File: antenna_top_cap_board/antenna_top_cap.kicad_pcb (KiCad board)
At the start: 4 copper layers, 100 x 100 mm, 61 parts, among them IC1 PCT2075DP,118, J1 Battery Charge Bypass, J10 USB_B_Micro, J11 USB_B_Micro, J13 USB_B_Micro, J14 BM04B-SRSS-TB(LF)(SN), J15 USB_B_Micro, J16 BM04B-SRSS-TB(LF)(SN), J17 BM04B-SRSS-TB(LF)(SN), J18 BM04B-SRSS-TB(LF)(SN)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

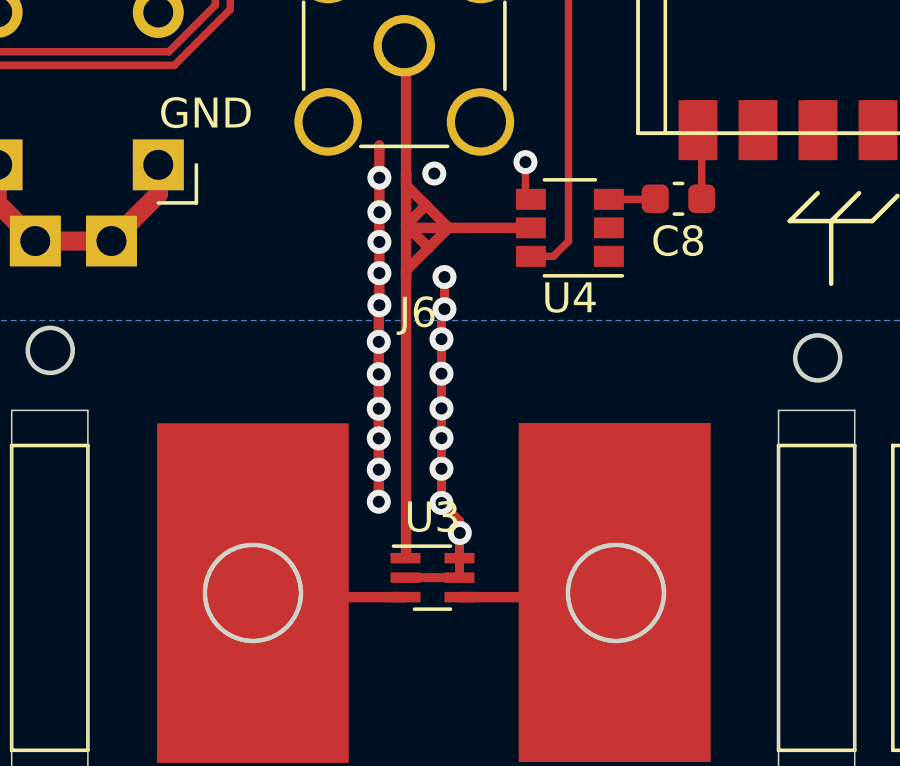
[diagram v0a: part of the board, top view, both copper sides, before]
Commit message: Added Jumper to Aux RF Line
Added an 0603 Jumper to break the Aux RF connection when not in use
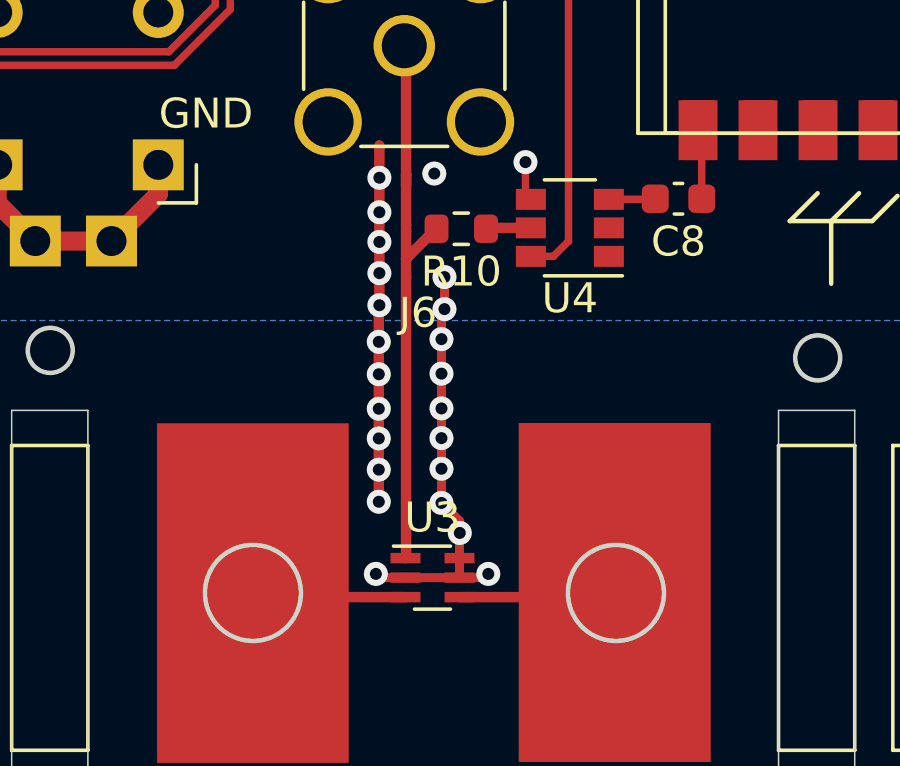
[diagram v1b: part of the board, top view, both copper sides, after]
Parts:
- added R10: DNI, Resistor_SMD:R_0603_1608Metric, F.Cu at (166.4, 123.8)
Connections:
- J5 pad 1: Balun -> Net-(J5-In)
- U3 pad 1: Balun -> Net-(J5-In)
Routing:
- net Balun: track 27.0 -> 1.51 mm
- net Net-(J5-In): track 0.00 -> 18.1 mm
- net GND: track 208.4 -> 210.5 mm, vias 38 -> 40

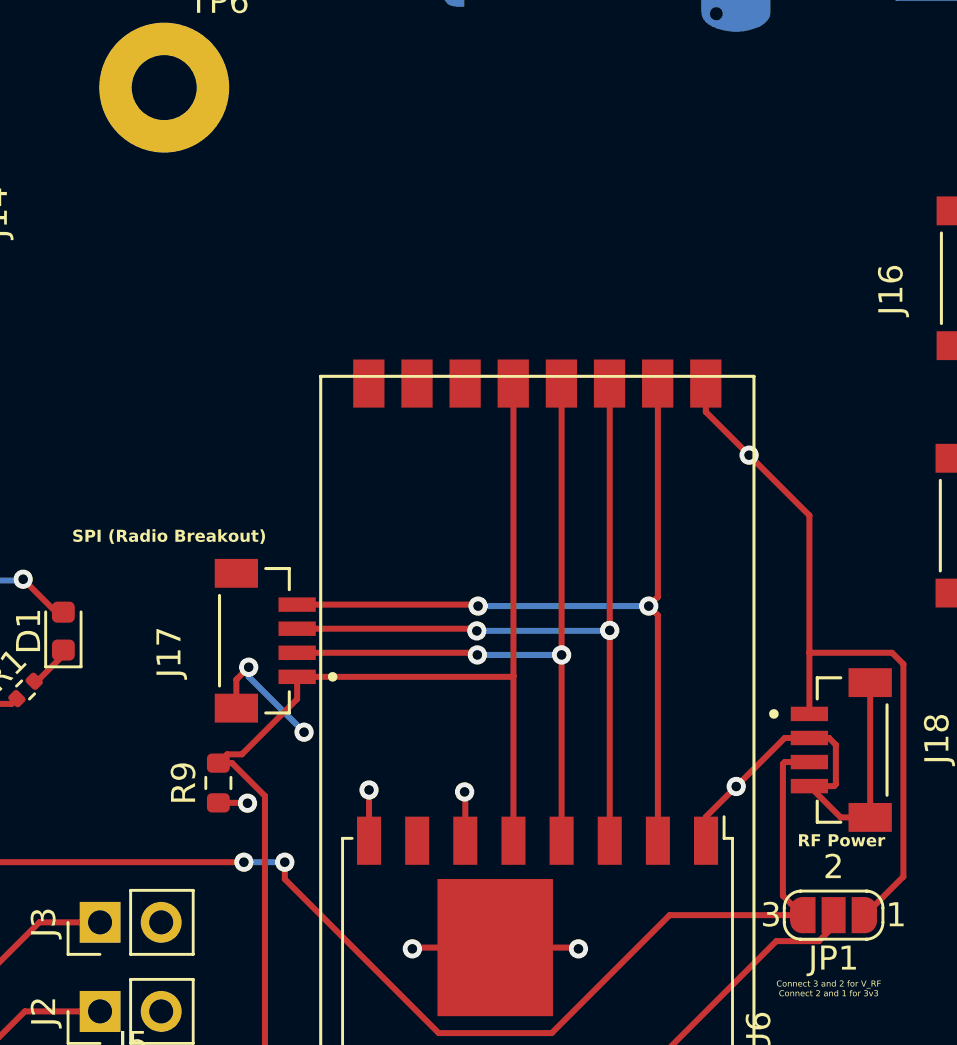
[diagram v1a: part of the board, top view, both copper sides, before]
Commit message: Relocated RF SPI Breakout
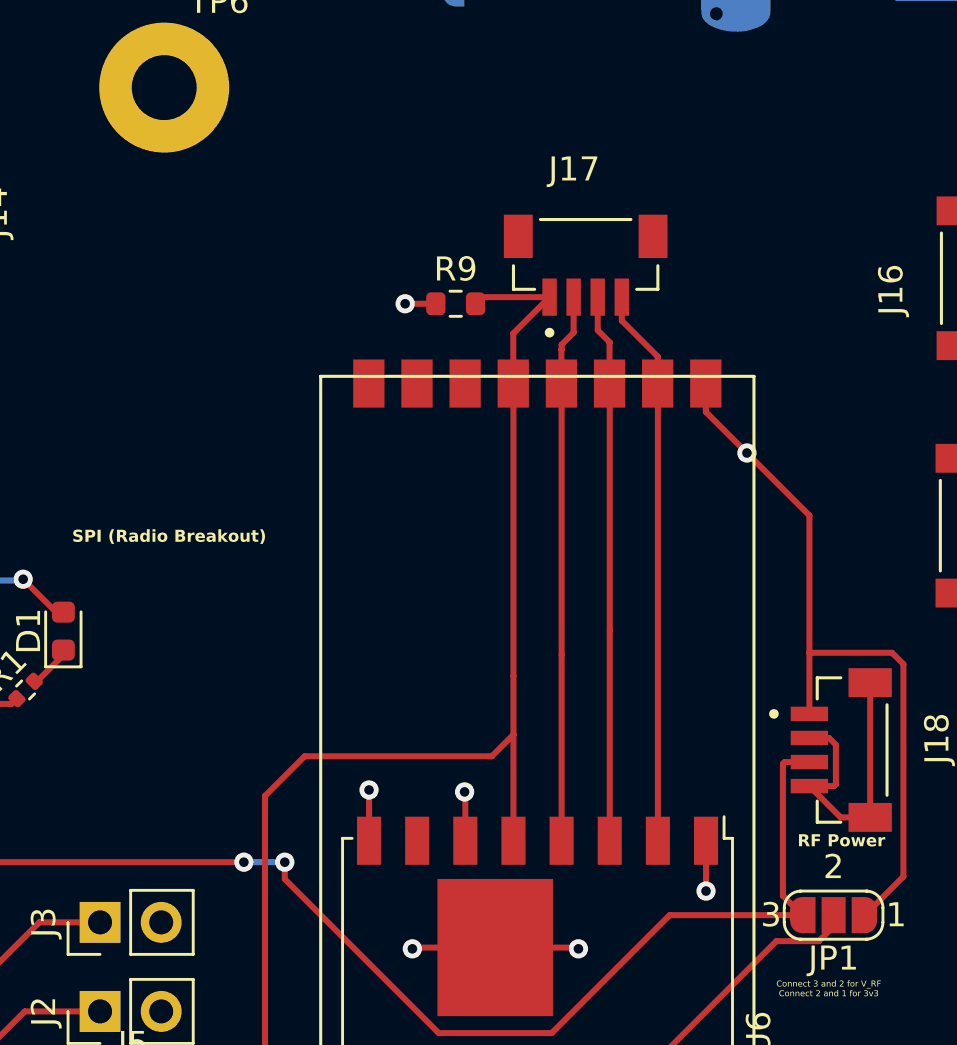
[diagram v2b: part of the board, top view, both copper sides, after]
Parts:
- moved R9 22.2 mm to (177.9, 82.2), turned to 0 degrees
- moved J17 22.2 mm to (183.3, 79.4), turned to 0 degrees
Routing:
- net SPI0_MISO: track 34.0 -> 23.2 mm, vias 2 -> 0
- net GND: track 210.5 -> 200.4 mm, vias 40 -> 38
- net SPI0_MOSI: track 32.0 -> 22.8 mm, vias 2 -> 0
- net SPI0_SCK: track 30.0 -> 22.8 mm, vias 2 -> 0
- net SPI0_CS0: track 58.8 -> 60.8 mm

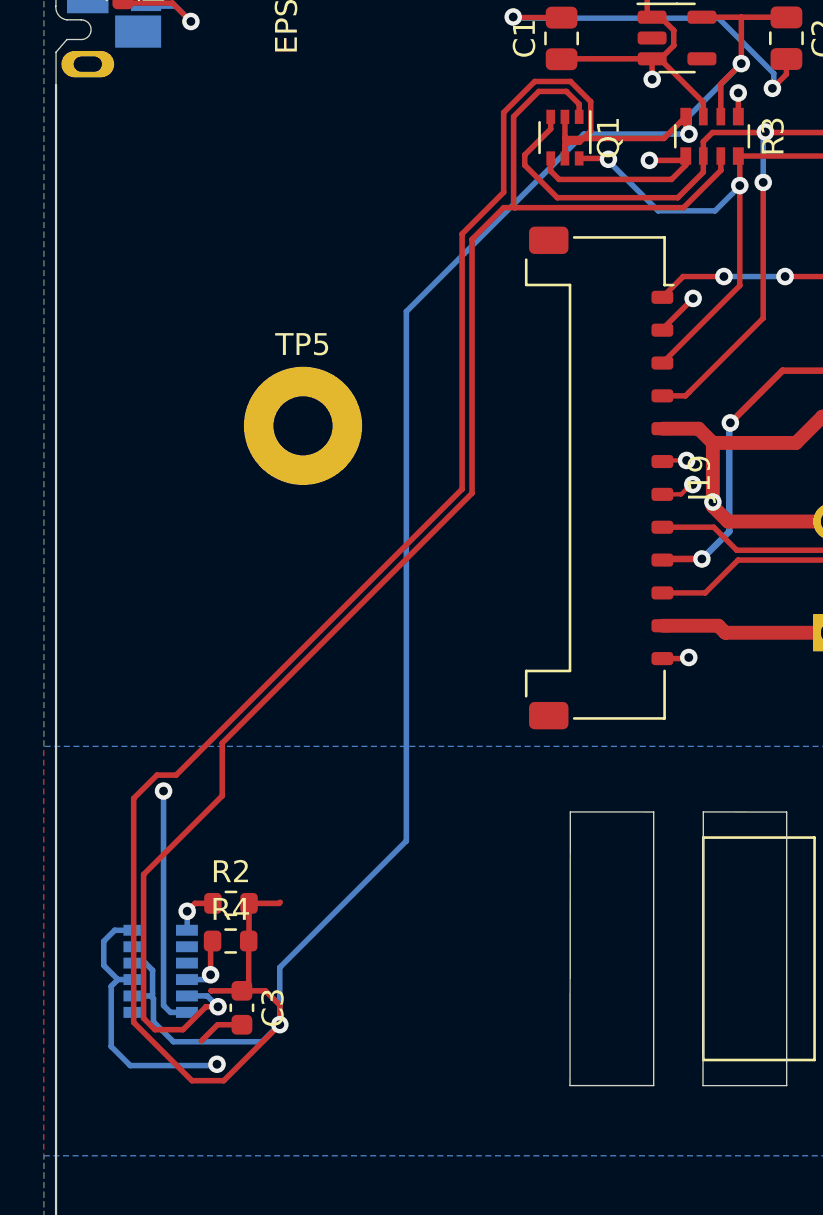
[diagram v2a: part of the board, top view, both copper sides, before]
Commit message: Removed redundant trace
For some reason there was both a 2.8V trace on the F.Cu and the B.Cu layers. Might be an artifact of the original design. The trace on the B.Cu layer was removed
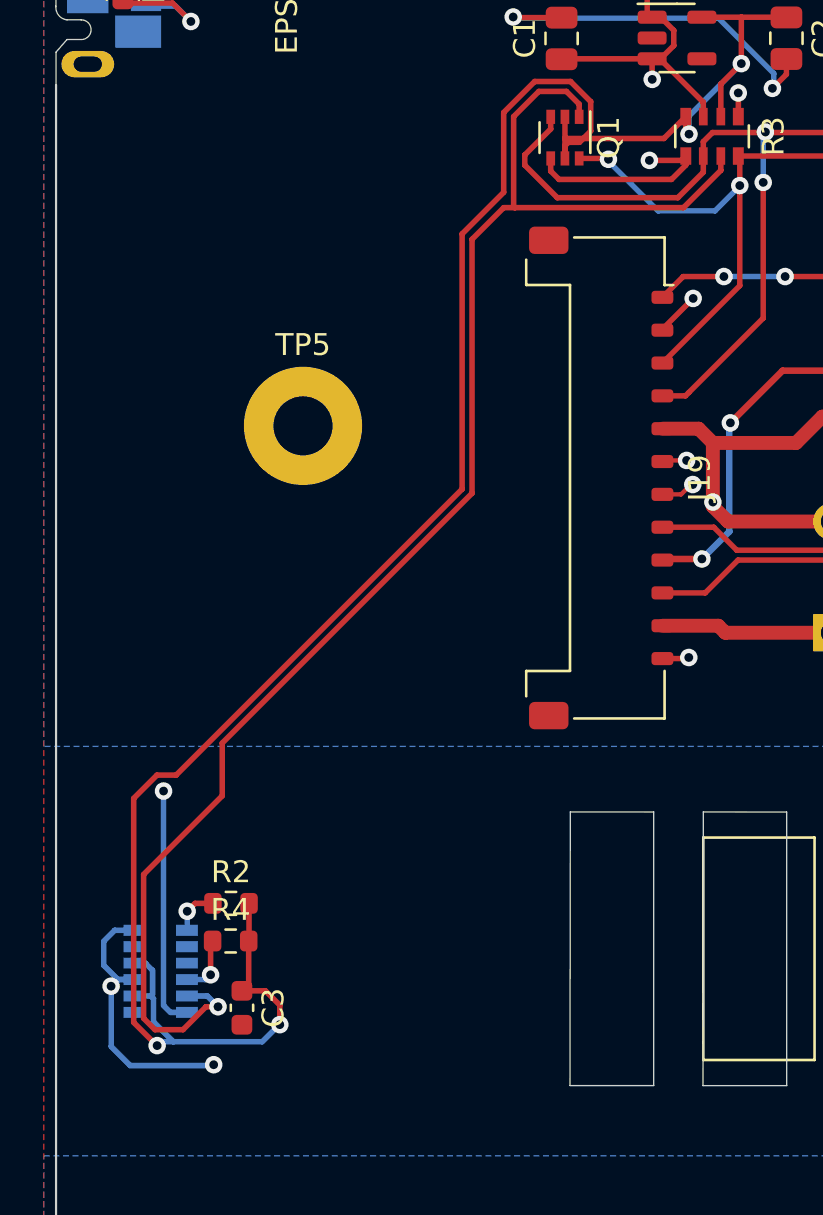
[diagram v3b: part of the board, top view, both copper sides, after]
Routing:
- net 2.8V: track 159.7 -> 99.1 mm, vias 3 -> 4
- net GND: track 200.4 -> 199.4 mm, vias 38 -> 39
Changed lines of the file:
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@@
-	)
-	(segment
-		(start 124.0358 139.5944)
-		(end 122.922039 139.5944)
-		(width 0.254)
-		(layer "F.Cu")
-		(net 1)
-	)
-	(segment
-		(start 122.922039 139.5944)
-		(end 122.183539 140.3329)
-		(width 0.254)
-		(layer "F.Cu")
-		(net 1)
 	)
 	(segment
@@
 	)
 	(via
-		(at 122.897421 141.398978)
+		(at 122.7458 141.4194)
 		(size 0.8)
 		(drill 0.4)
@@
 		(layers "F.Cu" "B.Cu")
 		(free yes)
+		(net 1)
+	)
+	(via
+		(at 118.058855 137.832994)
+		(size 0.8)
+		(drill 0.4)
+		(layers "F.Cu" "B.Cu")
 		(net 1)
 	)
@@
 	)
 	(segment
+		(start 119.1258 137.5294)
+		(end 118.362449 137.5294)
+		(width 0.254)
+		(layer "B.Cu")
+		(net 1)
+	)
+	(segment
 		(start 118.3718 137.5294)
 		(end 117.7258 136.8834)
@@
 		(end 136.488147 93.6194)
 		(width 0.25)
+		(layer "B.Cu")
+		(net 1)
+	)
+	(segment
+		(start 118.362449 137.5294)
+		(end 118.058855 137.832994)
+		(width 0.254)
 		(layer "B.Cu")
 		(net 1)
@@
 	)
 	(segment
-		(start 124.3608 134.0494)
-		(end 125.7358 134.0494)
-		(width 0.254)
-		(layer "F.Cu")
-		(net 9)
-	)
-	(segment
-		(start 125.7358 134.0494)
-		(end 125.7858 133.9994)
-		(width 0.254)
-		(layer "F.Cu")
-		(net 9)
-	)
-	(segment
 		(start 121.030748 128.1924)
 		(end 120.154666 128.1924)
@@
 	)
 	(segment
-		(start 121.753747 142.1494)
-		(end 123.2058 142.1494)
-		(width 0.254)
-		(layer "F.Cu")
-		(net 9)
-	)
-	(segment
 		(start 134.0918 115.131348)
 		(end 121.030748 128.1924)
@@
 	)
 	(segment
-		(start 124.0358 138.0444)
-		(end 122.631644 138.0444)
-		(width 0.254)
-		(layer "F.Cu")
-		(net 9)
-	)
-	(segment
 		(start 145.909484 96.630716)
 		(end 146.8458 95.6944)
@@
 	)
 	(segment
+		(start 119.0918 139.487453)
+		(end 120.150747 140.5464)
+		(width 0.254)
+		(layer "F.Cu")
+		(net 9)
+	)
+	(segment
 		(start 120.154666 128.1924)
 		(end 119.0918 129.255266)
@@
 	)
 	(segment
-		(start 119.0918 139.487453)
-		(end 121.753747 142.1494)
-		(width 0.254)
-		(layer "F.Cu")
-		(net 9)
-	)
-	(segment
-		(start 123.2058 142.1494)
-		(end 125.7658 139.5894)
+		(start 120.150747 140.5464)
+		(end 120.161883 140.5464)
 		(width 0.254)
 		(layer "F.Cu")
@@
 	)
 	(segment
-		(start 122.631644 138.0444)
-		(end 122.625302 138.038058)
-		(width 0.254)
-		(layer "F.Cu")
-		(net 9)
-	)
-	(segment
 		(start 138.789486 100.025224)
 		(end 138.789486 99.1144)
@@
 	)
 	(via
+		(at 120.161883 140.5464)
+		(size 0.8)
+		(drill 0.4)
+		(layers "F.Cu" "B.Cu")
+		(net 9)
+	)
+	(via
 		(at 125.7658 139.5894)
 		(size 0.8)
@@
 	)
 	(segment
-		(start 131.5458 107.0194)
-		(end 139.649475 98.915725)
-		(width 0.254)
-		(layer "B.Cu")
-		(net 9)
-	)
-	(segment
 		(start 119.8798 138.2794)
 		(end 119.9558 138.2034)
@@
 	)
 	(segment
-		(start 125.7658 136.977547)
-		(end 131.5458 131.197547)
-		(width 0.254)
-		(layer "B.Cu")
-		(net 9)
-	)
-	(segment
 		(start 144.4558 98.0844)
 		(end 144.4558 98.915725)
@@
 	)
 	(segment
-		(start 139.649475 98.915725)
-		(end 144.4558 98.915725)
-		(width 0.254)
-		(layer "B.Cu")
-		(net 9)
-	)
-	(segment
 		(start 125.74164 139.5894)
 		(end 125.7658 139.5894)
@@
 	)
 	(segment
-		(start 125.7658 139.5894)
-		(end 125.7658 136.977547)
-		(width 0.254)
-		(layer "B.Cu")
-		(net 9)
-	)
-	(segment
 		(start 119.9958 139.4594)
 		(end 120.9058 140.3694)
@@
 	)
 	(segment
-		(start 131.5458 131.197547)
-		(end 131.5458 107.0194)
+		(start 120.9058 140.3694)
+		(end 120.338883 140.3694)
 		(width 0.254)
 		(layer "B.Cu")
@@
 		(width 0.254)
 		(layer "B.Cu")
+		(net 9)
+	)
+	(segment
+		(start 120.338883 140.3694)
+		(end 120.161883 140.5464)
+		(width 0.254)
+		(layer "B.Cu")

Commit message: Updated Solder Mask
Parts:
- added G***: LOGO, LOGO, B.Cu at (195.9, 86.4)
- added G***: LOGO, LOGO, B.Cu at (172.6, 91.7)
- added G***: LOGO, LOGO, B.Cu at (179.2, 87.4)
- added G***: LOGO, LOGO, B.Cu at (184.9, 91.4)
- added G***: LOGO, LOGO, B.Cu at (184.7, 81.8)
- added G***: LOGO, LOGO, B.Cu at (173.2, 82.8)
- added REF**: Val**, mainboard:XYZ_cubesat-top, B.Cu at (197.8, 155.3)
- moved G*** 23.2 mm to (193.0, 117.3)
- moved G*** 5.85 mm to (179.4, 117.5)
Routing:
- net GND: track 199.4 -> 201.1 mm
- net 3.3V: track 62.9 -> 64.1 mm
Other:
- board text added: "3PySquared Antenna Development Board V1a Michael Pham | Nicole Maggard | Ernesto Montes"
- board text added: "THE PLEIADES FIVE"
